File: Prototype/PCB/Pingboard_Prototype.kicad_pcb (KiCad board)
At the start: 2 copper layers, 87.6 x 25.4 mm, 23 parts, among them J1 Conn_01x12, J2 Conn_01x12, SW1 SW_Push, SW2 SW_Push, SW3 SW_Push, SW4 SW_Push, U1 TLC59108xPW, U2 TLC59108xPW, U3 74LVC1G10

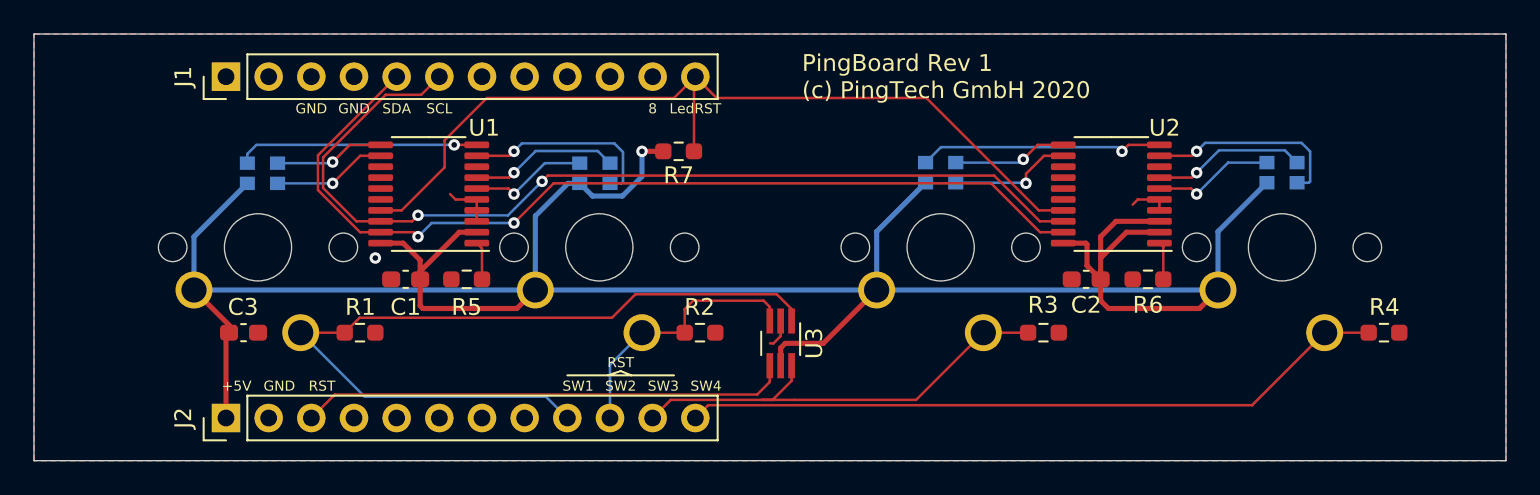
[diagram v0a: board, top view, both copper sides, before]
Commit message: Flip C1 and C2 to make a better VCC-GND loop
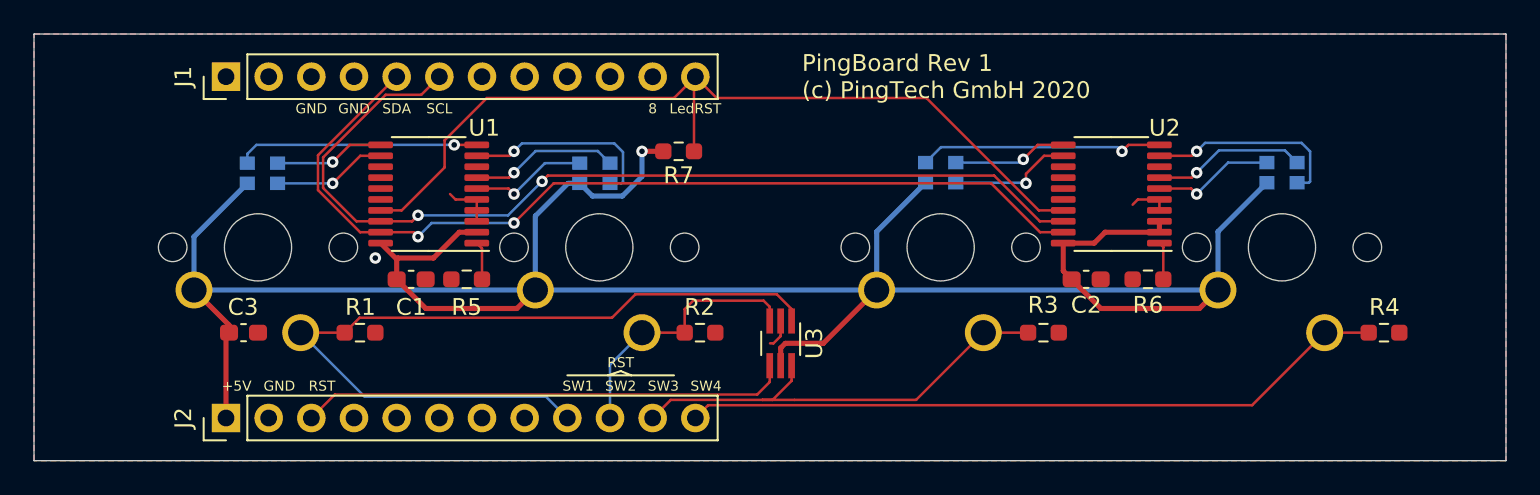
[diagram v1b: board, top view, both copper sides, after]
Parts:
- moved C1 0.33 mm to (122.1, 54.0), turned to 0 degrees
- turned C2 to 0 degrees
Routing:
- net VCC: track 156.8 -> 152.1 mm

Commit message: Add KiCAD project files in new format
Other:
- net class Default removed
- net class VCC removed
